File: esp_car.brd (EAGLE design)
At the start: 81.6 x 84 mm, 52 parts, among them IC2 LT1963ES8-3.3, SW2 SK-12D01

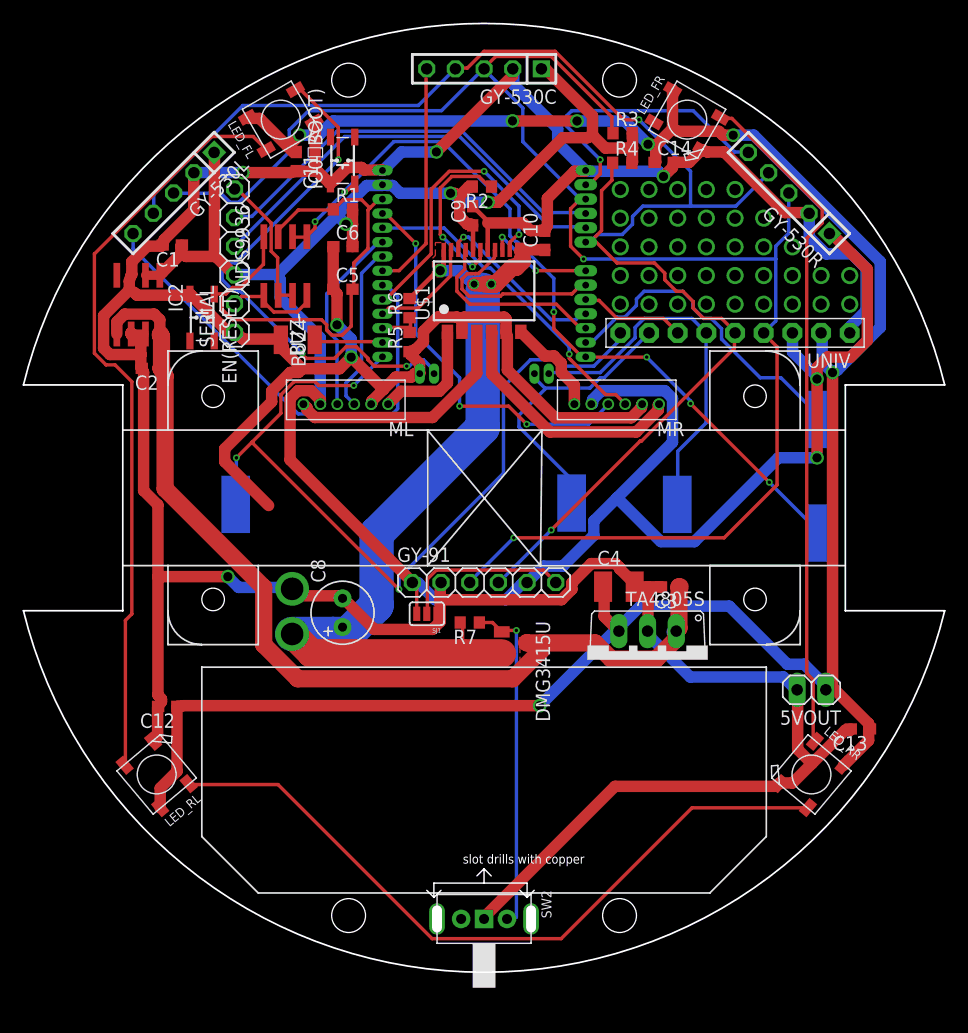
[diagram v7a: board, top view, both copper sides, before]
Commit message: esp32のviaの径設定ミス修正、NMOS向き修正、配線やり直し完了
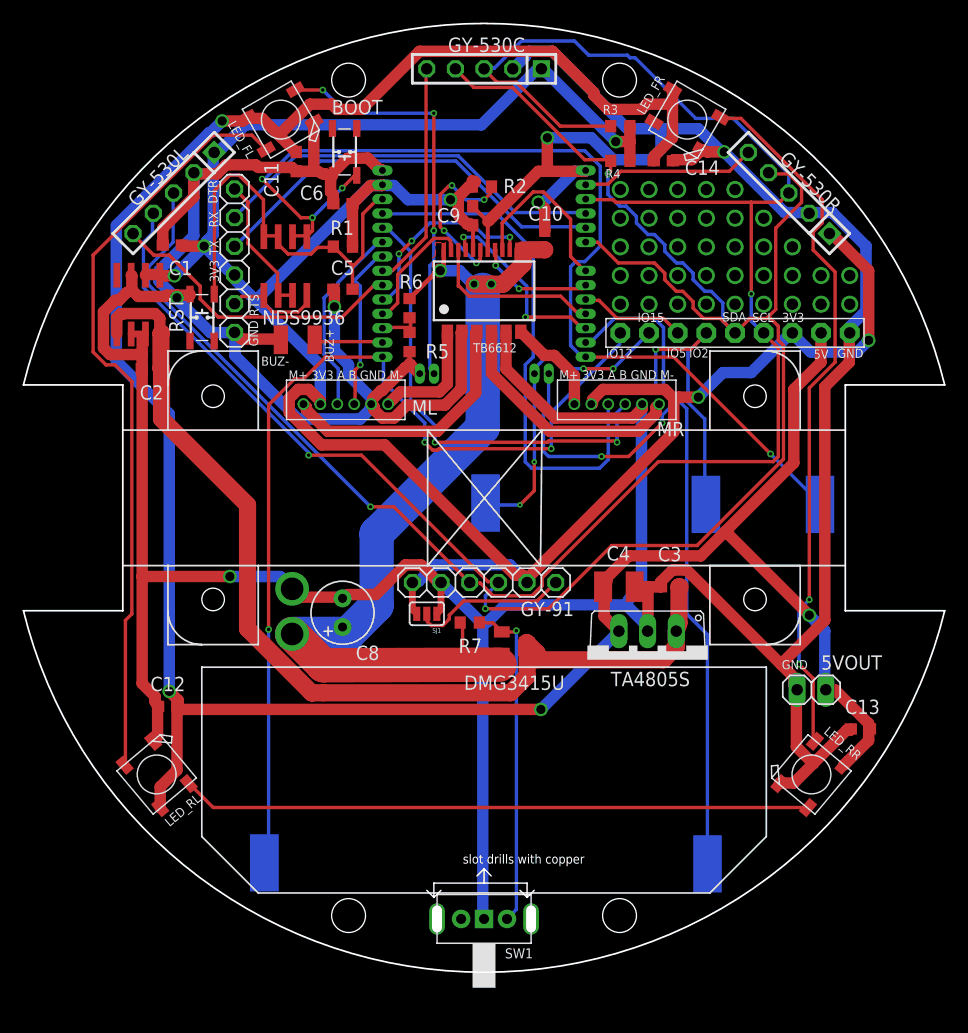
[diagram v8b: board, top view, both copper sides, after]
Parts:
- removed ESP32: ESP-WROOM-32_NOFLASH_PINHEAD, esp32 _my:ESP-WROOM-32_NOFLASH_PINHEAD
- removed IO0（BOOT): P-06185_SKRPACE010, Akizuki:SKRP
- added BOOT: P-06185_SKRPACE010, Akizuki:SKRP
- added TB6612: TB6612_NEW, adafruit_my:SSOP24_TB6612
- U$1: value TB6612_NEW -> ESP-WROOM-32_NOFLASH_PINHEAD; device adafruit_my:SSOP24_TB6612 -> esp32 _my:ESP-WROOM-32_NOFLASH_PINHEAD
- moved T0 40.7 mm to (59.8, 7.57)
- moved T5 31.9 mm to (20.5, 7.67)
- moved U$1 11.6 mm to (31.0, 51.0)
- moved T3 7.62 mm to (40.1, 39.5)
- moved C6 3.81 mm to (27.5, 66.1)
- moved R1 3.30 mm to (27.5, 62.2)
- moved T1 2.54 mm to (69.8, 39.4)
- moved T2 2.54 mm to (59.6, 39.4)
- moved R3 0.66 mm to (52.1, 72.9)
- moved R4 0.24 mm to (52.1, 69.8)
- moved C14 0.15 mm to (55.9, 69.8)
- renumbered EN(RESET) to RST, SW2 to SW1
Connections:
- net +3V3: now also TB6612.20, U$1.P$2; no longer ESP32.P$2, U$1.20
- net EN: now also U$1.P$3; no longer ESP32.P$3
- net ENCL_A: now also U$1.P$6; no longer ESP32.P$6
- net ENCL_B: now also U$1.P$7; no longer ESP32.P$7
- net ENCR_A: now also U$1.P$4; no longer ESP32.P$4
- net ENCR_B: now also U$1.P$5; no longer ESP32.P$5
- net GND: now also BOOT.2A, TB6612.0304, TB6612.0910, TB6612.18, U$1.P$1, U$1.P$15, U$1.P$38; no longer ESP32.P$1, ESP32.P$15, ESP32.P$38, IO0（BOOT).2A, U$1.0304, U$1.0910, U$1.18
- net I2C_SCL: now also U$1.P$36; no longer ESP32.P$36
- net I2C_SDA: now also U$1.P$33; no longer ESP32.P$33
- net IO0: now also BOOT.1A, U$1.P$25; no longer ESP32.P$25, IO0（BOOT).1A
- net IO12: now also U$1.P$14; no longer ESP32.P$14
- net IO15: now also U$1.P$23; no longer ESP32.P$23
- net IO2: now also U$1.P$24; no longer ESP32.P$24
- net IO27: now also U$1.P$12; no longer ESP32.P$12
- net IO4: now also U$1.P$26; no longer ESP32.P$26
- net IO5: now also U$1.P$29; no longer ESP32.P$29
- net ML-: now also TB6612.0102; no longer U$1.0102
- net ML_IN1: now also TB6612.21, U$1.P$27; no longer ESP32.P$27, U$1.21
- net ML_IN2: now also TB6612.22, U$1.P$28; no longer ESP32.P$28, U$1.22
- net ML_PWM: now also TB6612.23, U$1.P$11; no longer ESP32.P$11, U$1.23
- net MR+: now also TB6612.1112; no longer U$1.1112
- net MR-: now also TB6612.0708; no longer U$1.0708
- net MR_IN1: now also TB6612.17, U$1.P$30; no longer ESP32.P$30, U$1.17
- net MR_IN2: now also TB6612.16, U$1.P$31; no longer ESP32.P$31, U$1.16
- net MR_PWM: now also TB6612.15, U$1.P$10; no longer ESP32.P$10, U$1.15
- net N$18: now also U$1.P$16; no longer ESP32.P$16
- net N$19: now also U$1.P$9; no longer ESP32.P$9
- net N$3: now also U$1.P$8; no longer ESP32.P$8
- net N$38: now also TB6612.0506; no longer U$1.0506
- net N$5: now also U$1.P$37; no longer ESP32.P$37
- net N$7: now also TB6612.19; no longer U$1.19
- net N$8: now also U$1.P$13; no longer ESP32.P$13
- net RX: now also U$1.P$34; no longer ESP32.P$34
- net TX: now also U$1.P$35; no longer ESP32.P$35
- net VDD: now also TB6612.1314, TB6612.24; no longer U$1.1314, U$1.24
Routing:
- net GND: track 380.5 -> 442.8 mm
- net I2C_SDA: track 137.7 -> 172.7 mm, vias 2 -> 3
- net +5V: track 202.8 -> 231.7 mm, vias 7 -> 4
- net IO4: track 28.8 -> 57.3 mm
- net I2C_SCL: track 146.7 -> 171.7 mm
- net IO0: track 70.3 -> 91.6 mm, vias 6 -> 4
- net N$19: track 42.7 -> 27.1 mm
- net IO2: track 33.3 -> 48.0 mm, vias 0 -> 3
- net ENCR_B: track 28.6 -> 41.0 mm, vias 1 -> 2
- net ENCR_A: track 34.6 -> 46.6 mm, vias 3 -> 0
- net N$18: track 47.1 -> 36.5 mm
- net IO12: track 75.6 -> 86.0 mm
- net N$5: track 25.9 -> 15.6 mm, vias 1 -> 0
- net N$9: track 65.6 -> 55.7 mm
- net MR_PWM: track 25.7 -> 17.5 mm, vias 2 -> 3
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- removed copper zone on layer 1, net VCC
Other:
- board text added: "3V3"
- board text added: "5V"
- board text added: "DTR"
- board text added: "GND"
- board text added: "IO12"
- board text added: "IO15"
- board text added: "IO2"
- board text added: "IO5"
- board text added: "M+ 3V3 A B GND M-"
- board text added: "RTS"
- board text added: "RX"
- board text added: "SCL"
- board text added: "SDA"
- board text added: "TB6612"
- board text added: "TX"
